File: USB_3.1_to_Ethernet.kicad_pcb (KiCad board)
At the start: 4 copper layers, 77.2 x 25 mm, 79 parts, among them J1 RJ45_JK0654219, J2 USB3_A, U1 LAN7801_9JX, U2 93LC56B_SN, U4 TLV76733, U5 USBLC6-2P6, U6 TPS7A0212, U7 KSZ9031RNXCC, Y1 25MHz, Y2 25MHz

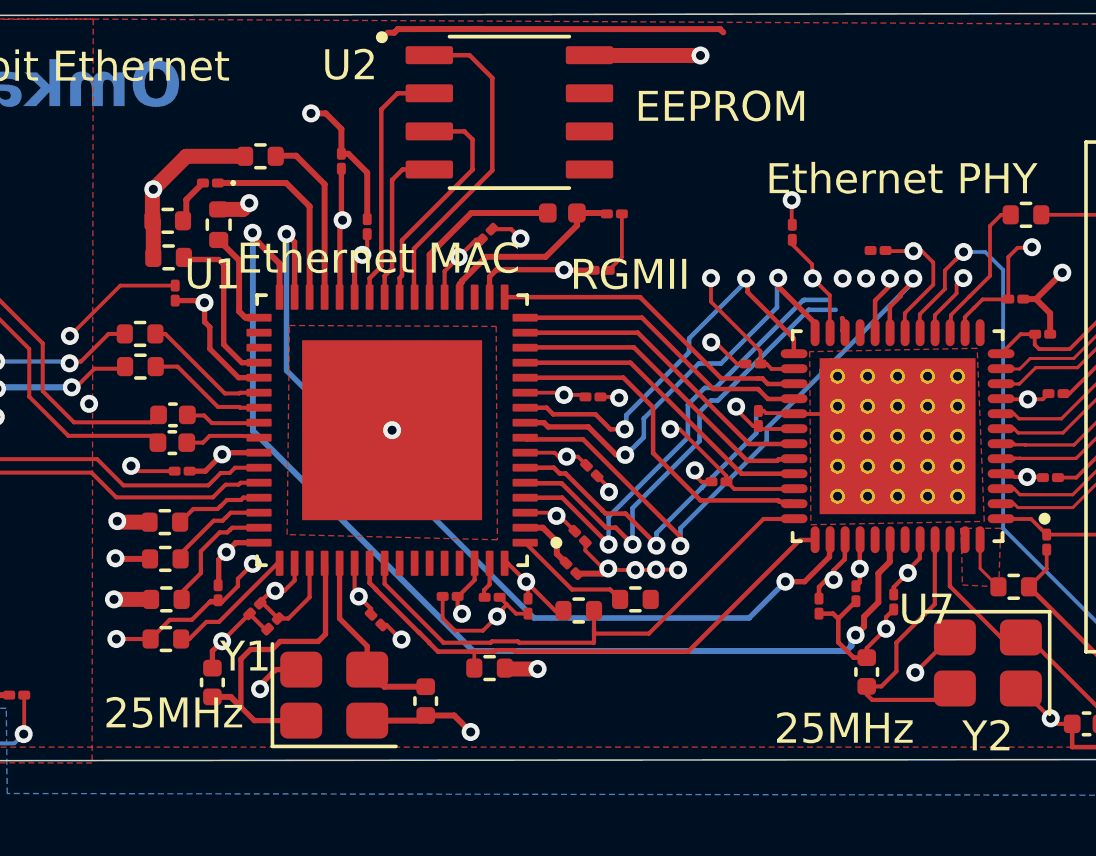
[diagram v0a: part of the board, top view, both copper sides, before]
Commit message: improved RGMII routing on bottom layer
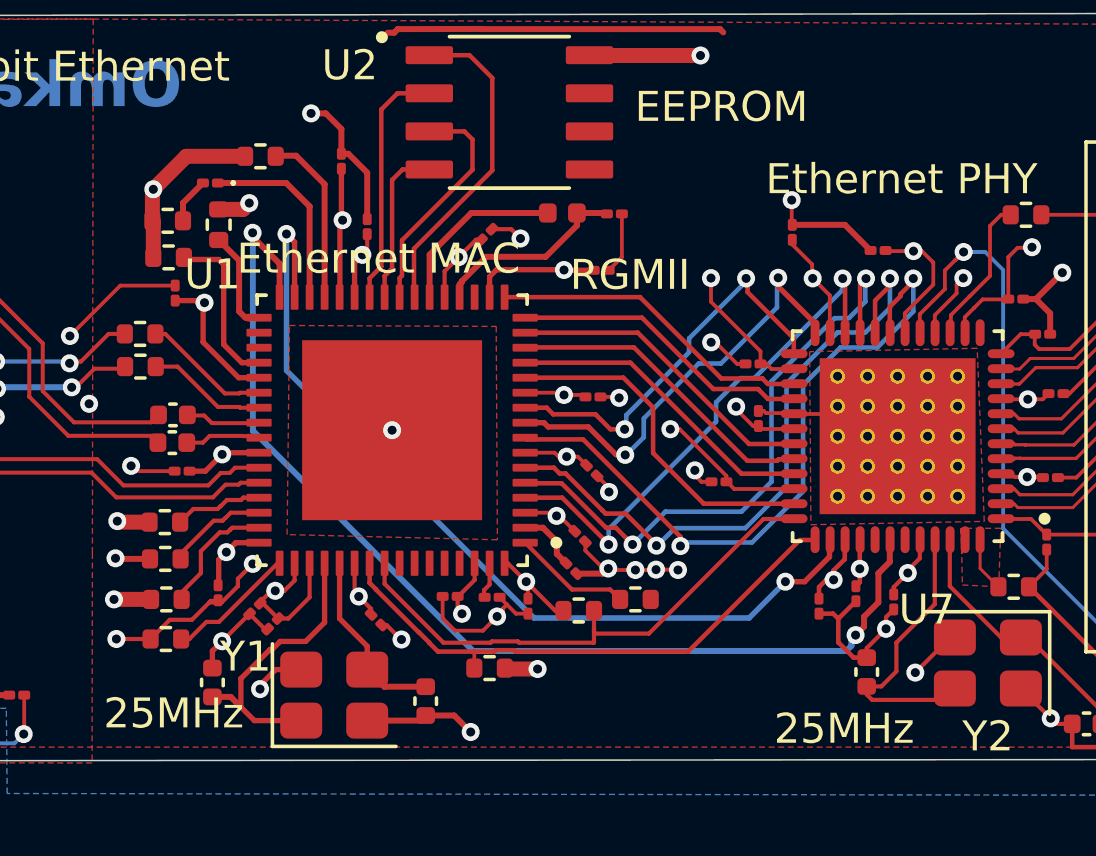
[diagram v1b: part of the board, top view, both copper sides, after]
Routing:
- net GND: track 147.3 -> 123.8 mm
- net /TXD1: track 13.6 -> 21.9 mm
- net /TXD2: track 15.7 -> 20.2 mm
- net 1v2_core: track 129.1 -> 133.1 mm
- net /TXD0: track 21.2 -> 23.2 mm
- net /TXD3: track 15.9 -> 17.7 mm
- net /XI_LAN: track 10.4 -> 9.78 mm

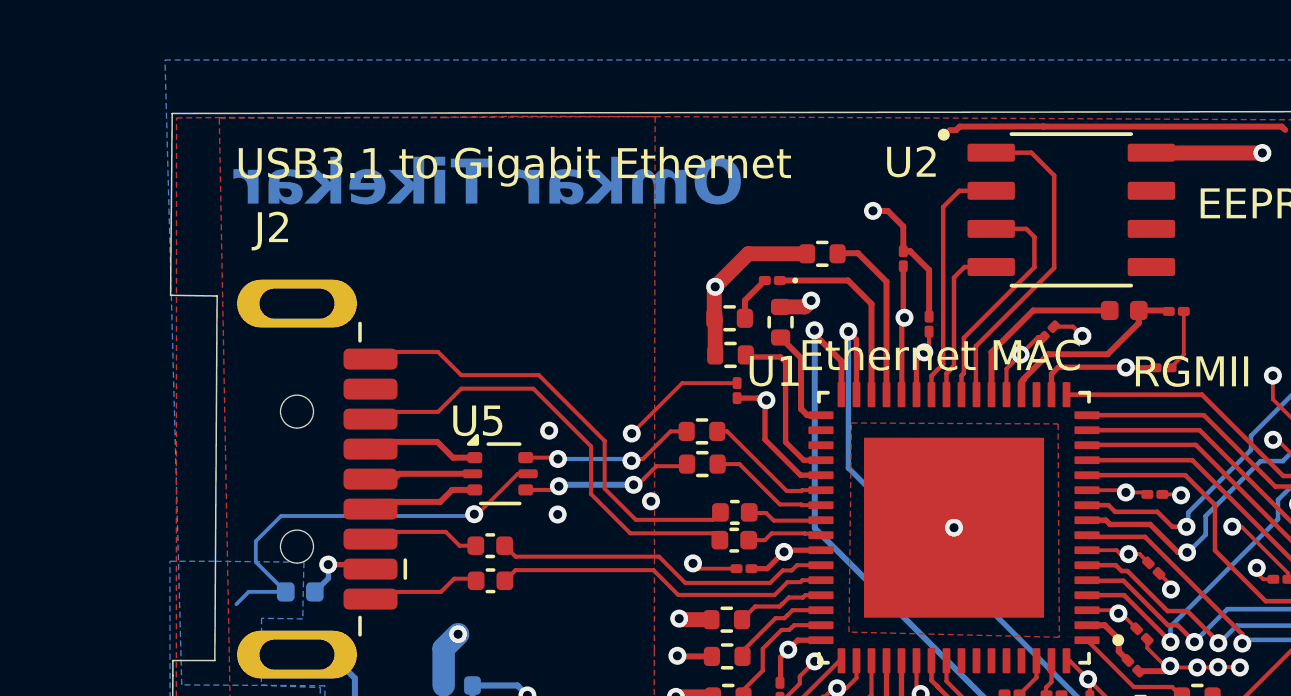
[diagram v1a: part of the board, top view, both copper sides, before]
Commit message: some minor changes in the routing
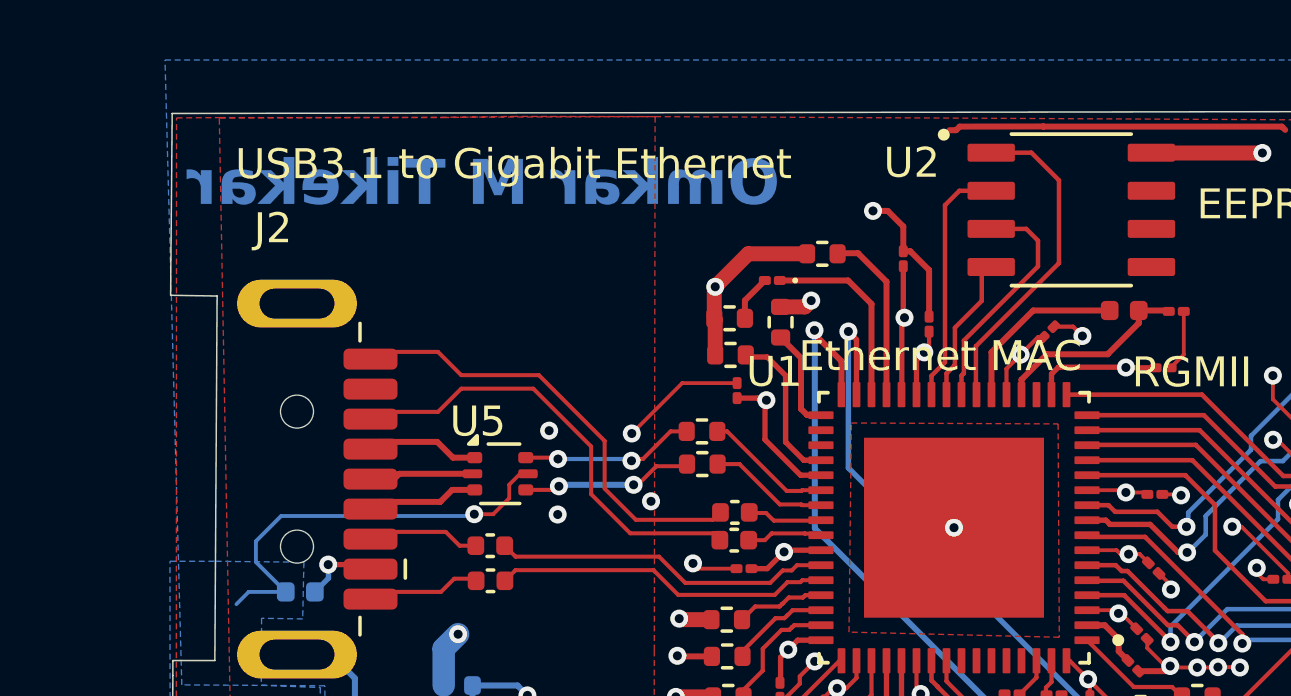
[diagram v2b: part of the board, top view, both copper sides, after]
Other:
- board text added: "Omkar M Tikekar"
- board text removed: "Omkar Tikekar"
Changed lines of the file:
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@@
 		(layer "Edge.Cuts")
 	)
-	(gr_text "Omkar Tikekar"
-		(at 77.3 53.34 0)
+	(gr_text "Omkar M Tikekar"
+		(at 78.5 53.35 0)
 		(layer "B.Cu")
 		(effects
@@
 	)
 	(segment
-		(start 89.42 58.18)
-		(end 87.438873 58.18)
-		(width 0.2)
-		(layer "F.Cu")
-		(net "Net-(U1-VDD12_SW_OUT)")
-	)
-	(segment
-		(start 91.43 56.72)
-		(end 91.46 56.75)
-		(width 0.2)
-		(layer "F.Cu")
-		(net "Net-(U1-VDD12_SW_OUT)")
-	)
-	(segment
-		(start 86.619999 58.998874)
-		(end 86.619999 59.030001)
+		(start 90.46 57.14)
+		(end 89.42 58.18)
 		(width 0.2)
 		(layer "F.Cu")
@@
 	)
 	(segment
-		(start 90.46 56.72)
-		(end 91.43 56.72)
+		(start 91.43 56.72)
+		(end 91.46 56.75)
 		(width 0.2)
 		(layer "F.Cu")
@@
 	)
 	(segment
-		(start 90.46 57.14)
-		(end 89.42 58.18)
+		(start 87.395 58.18)
+		(end 86.549999 59.025001)
 		(width 0.2)
 		(layer "F.Cu")
@@
 	)
 	(segment
-		(start 86.549999 59.100001)
-		(end 86.549999 59.525)
+		(start 89.42 58.18)
+		(end 87.395 58.18)
 		(width 0.2)
 		(layer "F.Cu")
@@
 	)
 	(segment
-		(start 87.438873 58.18)
-		(end 86.619999 58.998874)
+		(start 90.46 56.72)
+		(end 91.43 56.72)
 		(width 0.2)
 		(layer "F.Cu")
@@
 	)
 	(segment
-		(start 86.619999 59.030001)
-		(end 86.549999 59.100001)
+		(start 86.549999 59.025001)
+		(end 86.549999 59.525)
 		(width 0.2)
 		(layer "F.Cu")
@@
 	)
 	(segment
-		(start 87.64 55.3)
-		(end 87.64 52.22)
+		(start 87.8 52.38)
+		(end 86.88 51.46)
 		(width 0.15)
 		(layer "F.Cu")
@@
 	)
 	(segment
-		(start 87.64 52.22)
-		(end 86.88 51.46)
+		(start 87.8 55.14)
+		(end 87.8 52.38)
 		(width 0.15)
 		(layer "F.Cu")
@@
 	)
 	(segment
-		(start 85.03 59.505)
-		(end 85.03 57.91)
+		(start 85.03 57.91)
+		(end 87.8 55.14)
 		(width 0.15)
 		(layer "F.Cu")
@@
 	)
 	(segment
-		(start 85.03 57.91)
-		(end 87.64 55.3)
+		(start 85.03 59.505)
+		(end 85.03 57.91)
 		(width 0.15)
 		(layer "F.Cu")
@@
 	)
 	(segment
-		(start 84.549999 58.890001)
-		(end 84.549999 59.525)
+		(start 85.54 54)
+		(end 86.71 54)
 		(width 0.15)
 		(layer "F.Cu")
@@
 	)
 	(segment
-		(start 85.54 54)
-		(end 86.71 54)
+		(start 87.1 54.39)
+		(end 87.1 55.25)
 		(width 0.15)
 		(layer "F.Cu")
@@
 	)
 	(segment
-		(start 86.98 54.27)
-		(end 86.98 55.28)
+		(start 84.549999 58.890001)
+		(end 84.549999 59.525)
 		(width 0.15)
 		(layer "F.Cu")
@@
 	)
 	(segment
-		(start 86.71 54)
-		(end 86.98 54.27)
+		(start 87.1 55.25)
+		(end 84.63 57.72)
 		(width 0.15)
 		(layer "F.Cu")
@@
 	)
 	(segment
-		(start 86.98 55.28)
-		(end 84.63 57.63)
+		(start 84.63 57.72)
+		(end 84.63 58.81)
 		(width 0.15)
 		(layer "F.Cu")
@@
 	)
 	(segment
-		(start 84.63 57.63)
-		(end 84.63 58.81)
+		(start 86.71 54)
+		(end 87.1 54.39)
 		(width 0.15)
 		(layer "F.Cu")
@@
 	)
 	(segment
-		(start 85.54 55.27)
-		(end 84.65 55.27)
+		(start 85.225 56.4)
+		(end 84.33 57.295)
+		(width 0.15)
+		(layer "F.Cu")
+		(net "/DO")
+	)
+	(segment
+		(start 84.33 57.295)
+		(end 84.33 58.54)
 		(width 0.15)
 		(layer "F.Cu")
@@
 	)
 	(segment
-		(start 84.3 58.57)
+		(start 84.33 58.54)
 		(end 84.05 58.82)
 		(width 0.15)
@@
 	)
 	(segment
-		(start 84.65 55.27)
-		(end 84.3 55.62)
+		(start 85.35 55.27)
+		(end 85.225 55.395)
 		(width 0.15)
 		(layer "F.Cu")
@@
 	)
 	(segment
-		(start 84.3 55.62)
-		(end 84.3 58.57)
+		(start 85.54 55.27)
+		(end 85.35 55.27)
+		(width 0.15)
+		(layer "F.Cu")
+		(net "/DO")
+	)
+	(segment
+		(start 85.225 55.395)
+		(end 85.225 56.4)
 		(width 0.15)
 		(layer "F.Cu")
@@
 	)
 	(segment
-		(start 83.549998 58.895738)
-		(end 83.549998 59.525)
+		(start 85.54 52.73)
+		(end 84.48 52.73)
 		(width 0.15)
 		(layer "F.Cu")
@@
 	)
 	(segment
-		(start 84.48 52.73)
-		(end 83.94 53.27)
+		(start 84 53.21)
+		(end 84 58.445736)
 		(width 0.15)
 		(layer "F.Cu")
@@
 	)
 	(segment
-		(start 83.94 58.505736)
-		(end 83.549998 58.895738)
+		(start 84.48 52.73)
+		(end 84 53.21)
 		(width 0.15)
 		(layer "F.Cu")
@@
 	)
 	(segment
-		(start 83.94 53.27)
-		(end 83.94 58.505736)
+		(start 84 58.445736)
+		(end 83.549998 58.895738)
 		(width 0.15)
 		(layer "F.Cu")
@@
 	)
 	(segment
-		(start 85.54 52.73)
-		(end 84.48 52.73)
+		(start 83.549998 58.895738)
+		(end 83.549998 59.525)
 		(width 0.15)
 		(layer "F.Cu")
@@
 	)
 	(segment
-		(start 78.68712 58.43712)
-		(end 78.52 58.27)
+		(start 77.49 58.27)
+		(end 77.42 58.2)
 		(width 0.18)
 		(layer "F.Cu")
@@
 	)
 	(segment
-		(start 78.68712 61.105564)
-		(end 78.68712 58.43712)
+		(start 78.68712 58.88712)
+		(end 78.07 58.27)
 		(width 0.18)
 		(layer "F.Cu")
@@
 	)
 	(segment
-		(start 77.49 58.27)
-		(end 77.42 58.2)
+		(start 78.07 58.27)
+		(end 77.49 58.27)
 		(width 0.18)
 		(layer "F.Cu")
@@
 	)
 	(segment
-		(start 79.864999 61.71)
-		(end 79.291556 61.71)
+		(start 78.68712 61.105564)
+		(end 78.68712 58.88712)
 		(width 0.18)
 		(layer "F.Cu")
@@
 	)
 	(segment
-		(start 78.52 58.27)
-		(end 77.49 58.27)
+		(start 79.291556 61.71)
+		(end 78.68712 61.105564)
 		(width 0.18)
 		(layer "F.Cu")
@@
 	)
 	(segment
-		(start 79.291556 61.71)
-		(end 78.68712 61.105564)
+		(start 79.864999 61.71)
+		(end 79.291556 61.71)
 		(width 0.18)
 		(layer "F.Cu")
@@
 	)
 	(segment
-		(start 68.414248 63.51)
-		(end 69.761748 62.1625)
+		(start 69.8375 62.1625)
+		(end 70.1 62.1625)
 		(width 0.127)
 		(layer "F.Cu")
@@
 	)
 	(segment
-		(start 69.761748 62.1625)
-		(end 70.1 62.1625)
+		(start 68.94 63.51)
+		(end 69.475 62.975)
 		(width 0.127)
 		(layer "F.Cu")
@@
 	(segment
 		(start 68.31 63.51)
-		(end 68.414248 63.51)
+		(end 68.94 63.51)
+		(width 0.127)
+		(layer "F.Cu")
+		(net "+5V")
+	)
+	(segment
+		(start 69.475 62.525)
+		(end 69.8375 62.1625)
+		(width 0.127)
+		(layer "F.Cu")
+		(net "+5V")
+	)
+	(segment
+		(start 69.475 62.975)
+		(end 69.475 62.525)
 		(width 0.127)
 		(layer "F.Cu")
